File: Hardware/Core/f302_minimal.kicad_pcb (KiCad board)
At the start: 2 copper layers, 56.8 x 38.5 mm, 43 parts, among them J1 USB_B_Micro, J2 Conn_02x10_Odd_Even, J3 Conn_02x10_Odd_Even, J4 Conn_01x04, SW1 SW_Push, U1 USBLC6-2SC6, U2 AMS1117-3.3, U3 LP5907MFX-3.3, U4 QMI8658C, U5 STM32F302C8Tx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

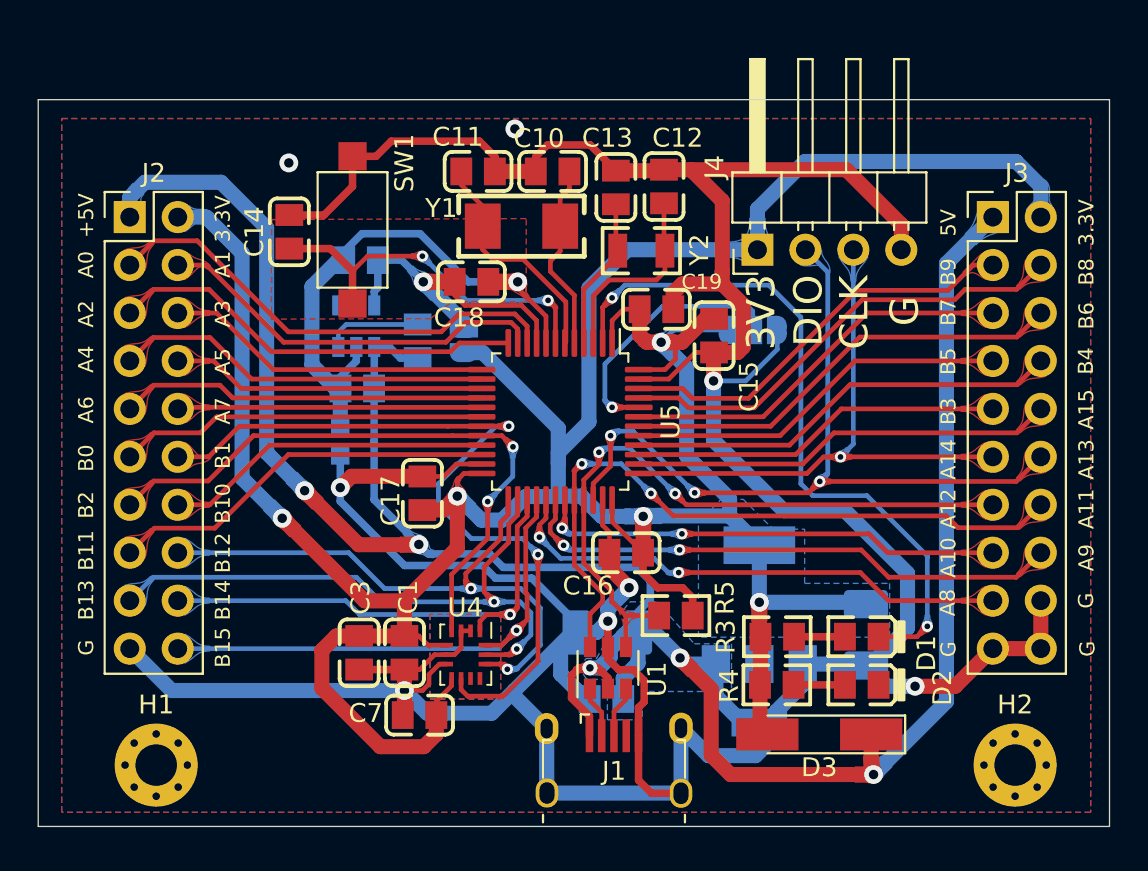
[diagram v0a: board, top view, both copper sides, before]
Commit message: update hardware, add eskf code, bug fix
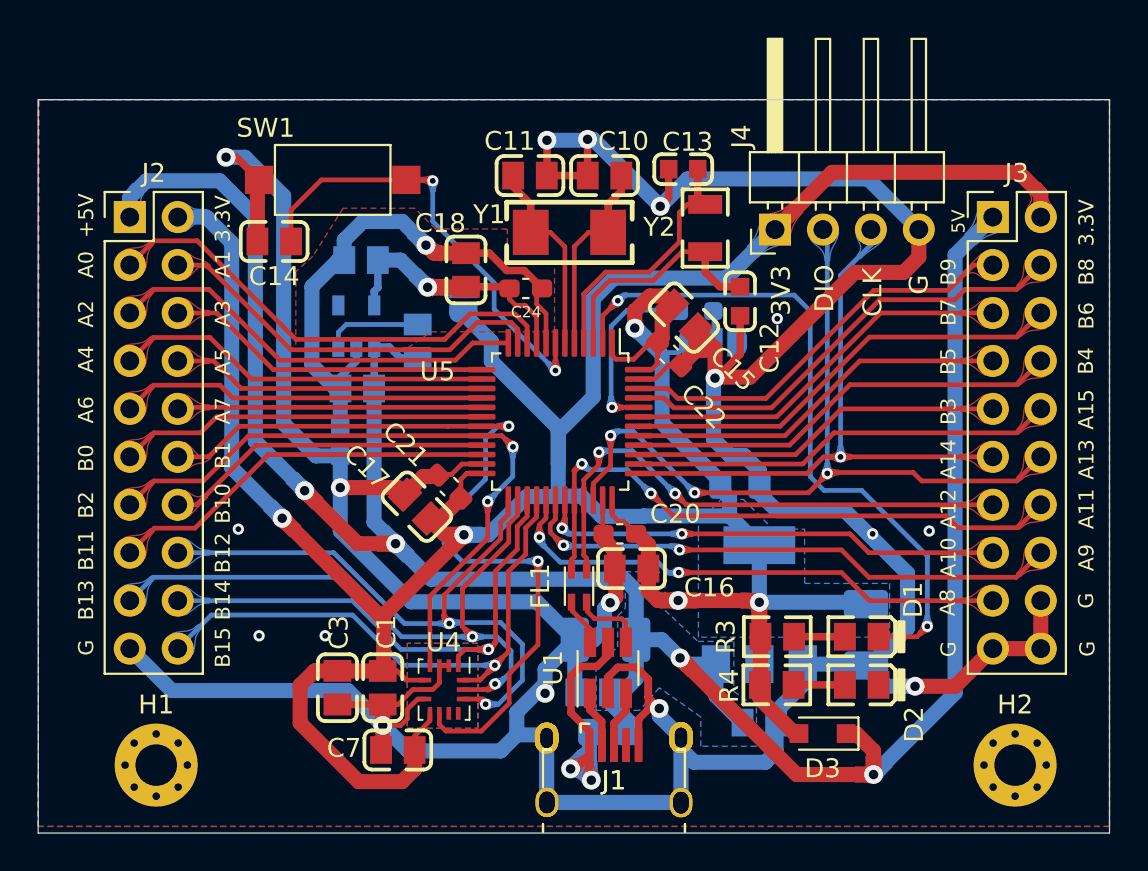
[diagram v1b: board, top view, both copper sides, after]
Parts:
- removed C19: 0805_100nF_104_10%_50V, lc_lib:0805_C
- added C20: 10nF, Capacitor_SMD:C_0603_1608Metric_Pad1.08x0.95mm_HandSolder, F.Cu at (104.0, 101.9)
- added C21: 10nF, Capacitor_SMD:C_0603_1608Metric_Pad1.08x0.95mm_HandSolder, F.Cu at (94.9, 99.4)
- added C22: 10nF, Capacitor_SMD:C_0603_1608Metric_Pad1.08x0.95mm_HandSolder, F.Cu at (106.6, 92.4)
- added C24: 10nF, Capacitor_SMD:C_0603_1608Metric_Pad1.08x0.95mm_HandSolder, F.Cu at (99.0, 88.9)
- added C25: 4.7uF, Capacitor_SMD:C_0805_2012Metric_Pad1.18x1.45mm_HandSolder, B.Cu at (110.3, 99.3)
- added FB1: FB, Resistor_SMD:R_0805_2012Metric_Pad1.20x1.40mm_HandSolder, B.Cu at (103.3, 112.4)
- added FL1: EMI_Filter_LL, Core:DLW21SN900SQ2L, F.Cu at (101.8, 104.7)
- added J1: USB_B_Micro, Connector_USB:USB_MicroB, F.Cu at (103.7, 115.5)
- C12, C13: footprint lc_lib:0805_C -> lc_lib:0603_C
- C18: value 0805_100nF_104_10%_50V -> 1uF
- D3: value 1N4148 -> CUS10S30; footprint Diode_SMD:D_MiniMELF_Handsoldering -> Diode_SMD:D_SOD-323_HandSoldering
- R5: value 0805_1.5KΩ__1501_1% -> 10k; footprint lc_lib:0805_R -> Resistor_SMD:R_0603_1608Metric_Pad0.98x0.95mm_HandSolder; moved to B.Cu
- U1: footprint Package_TO_SOT_SMD:SOT-23-6 -> Package_TO_SOT_SMD:SOT-23-6_Handsoldering
- moved R5 16.2 mm to (108.0, 90.1)
- moved C12 7.29 mm to (110.3, 89.6), turned to 90 degrees
- moved C13 3.70 mm to (107.3, 82.6), turned to 0 degrees
- moved Y2 3.59 mm to (108.5, 85.7), turned to 90 degrees
- moved SW1 2.85 mm to (88.8, 83.2), turned to 0 degrees
- moved C10 2.76 mm to (103.2, 82.9)
- moved C11 2.76 mm to (99.2, 82.9)
- moved Y1 2.56 mm to (101.3, 85.9)
- moved JP2 2.20 mm to (108.9, 91.8)
- moved U4 2.18 mm to (94.7, 110.2)
- moved C3 2.18 mm to (89.0, 110.0)
- moved C1 2.18 mm to (91.4, 110.0)
- moved C7 2.18 mm to (92.2, 113.3)
- moved JP1 2.09 mm to (95.7, 89.6)
- moved C15 1.86 mm to (107.4, 90.4), turned to 315 degrees
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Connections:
- J1 pad 1: +5V -> Net-(FB1-Pad2)
- JP2 pad 2: /BOOT -> Net-(JP2-Pad2)
- R5 pad 1: +3V3 -> Net-(JP2-Pad2)
- R5 pad 2: /PA12 -> /BOOT
- U1 pad 2: +5V -> GNDD
- U1 pad 4: /PA12 -> Net-(FL1-Pad4)
- U1 pad 5: GNDD -> Net-(FB1-Pad2)
- U1 pad 6: /PA11 -> Net-(FL1-Pad1)
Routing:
- net GNDD: track 226.0 -> 245.3 mm, vias 8 -> 17
- net Net-(FB1-Pad2): track 0.00 -> 16.6 mm, vias 0 -> 2
- net +5V: track 132.2 -> 123.1 mm, vias 5 -> 4
- net /PA12: track 35.5 -> 28.7 mm
- net /OSC32_OUT: track 8.13 -> 13.9 mm
- net /PA11: track 37.0 -> 32.1 mm
- net /BOOT: track 14.1 -> 9.64 mm
- net /RST: track 19.6 -> 24.1 mm
- net Net-(FL1-Pad4): track 0.00 -> 3.82 mm
- net /OSC_N: track 13.8 -> 10.6 mm
- net /IMU_INT2: track 41.9 -> 44.7 mm
- net /PB15: track 27.8 -> 30.3 mm
- net Net-(FL1-Pad1): track 0.00 -> 2.52 mm
- net /PB12: track 31.8 -> 34.1 mm
- net /IMU_INT1: track 33.2 -> 35.5 mm
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- removed copper zone on F.Cu, net /PA12
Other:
- board size 56.8 x 38.5 mm -> 56.8 x 38.8 mm
- board text added: "3.3VA-D"
- board text added: "BOOT"
